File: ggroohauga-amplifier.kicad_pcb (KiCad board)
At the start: 2 copper layers, 90 x 31 mm, 9 parts

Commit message: Ground unused GPIOs
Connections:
- A-C1 pad 2: GND -> GPIO_L11_C11_M15
- A-C2 pad 2: GND -> GPIO_L11_C11_M15
- A-J1 pad 0: GND -> GPIO_L11_C11_M15
- A-J1 pad 6: GND -> GPIO_L11_C11_M15
- A-U1 pad 15: GND -> GPIO_L11_C11_M15
- A-U1 pad 2: GND -> GPIO_L11_C11_M15
- A-U1 pad 8: GND -> GPIO_L11_C11_M15
- A-U1 pad 9: GND -> GPIO_L11_C11_M15
- S3L1 pad 11: GPIO_L18_C18_M9 -> GPIO_L11_C11_M15
- S3L1 pad 18: GPIO_L12_C12_M16 -> GPIO_L11_C11_M15
- S3L1 pad 7: GND -> GPIO_L11_C11_M15
- S3L1 pad 8: GND -> GPIO_L11_C11_M15
- S3L1 pad 9: GND -> GPIO_L11_C11_M15
- S3R1 pad 1: GND -> GPIO_L11_C11_M15
- S3R1 pad 14: GPIO_L47_C47_M35 -> GPIO_L11_C11_M15
- S3R1 pad 15: GPIO_L21_C21_M21 -> GPIO_L11_C11_M15
- S3R1 pad 7: GPIO_L41_C41_M42 -> GPIO_L11_C11_M15
- S3R1 pad 9: GPIO_L39_C39_M40 -> GPIO_L11_C11_M15
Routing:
- net GPIO_L11_C11_M15: track 0.00 -> 9.52 mm, vias 0 -> 3
- net GND: track 9.52 -> 0.00 mm, vias 3 -> 0
- added copper zone on B.Cu, net GPIO_L11_C11_M15
- added copper zone on F.Cu, net GPIO_L11_C11_M15
- removed copper zone on B.Cu, net GND
- removed copper zone on F.Cu, net GND

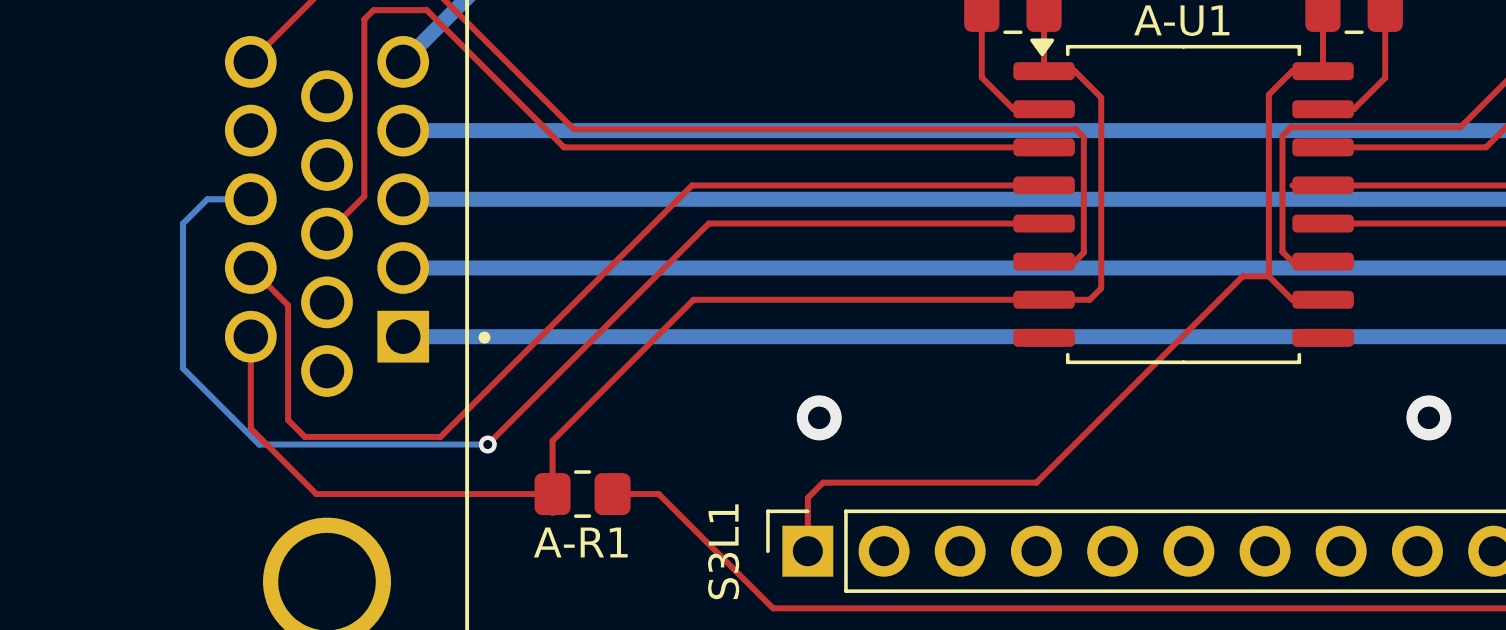
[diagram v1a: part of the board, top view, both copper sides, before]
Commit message: Move bridge text out of the way of vias and cleanup tracks
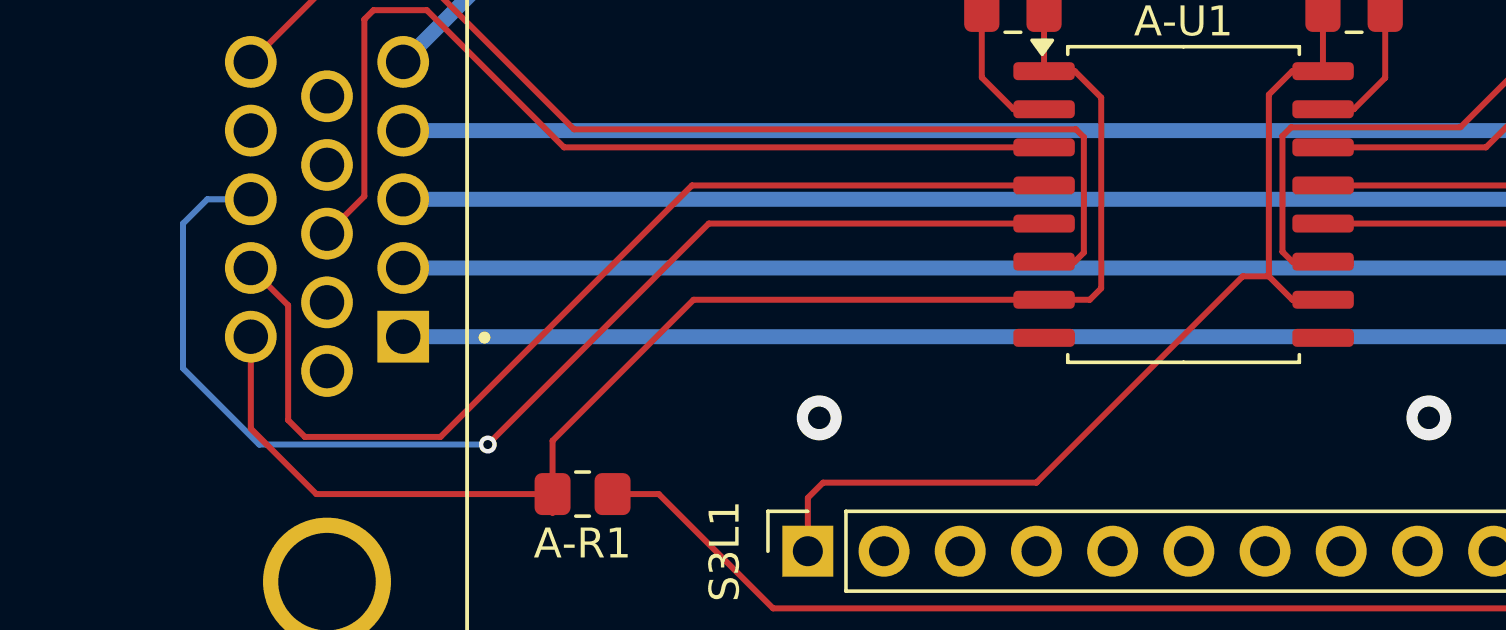
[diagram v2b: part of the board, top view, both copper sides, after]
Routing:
- net /Common/GPIO_L9_C9_M13/AMP_TX: track 25.2 -> 24.2 mm
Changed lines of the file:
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@@
 	)
 	(segment
-		(start 63.246 73.914)
-		(end 62.357 73.025)
-		(width 0.2)
-		(layer "B.Cu")
-		(net 6)
-	)
-	(segment
-		(start 62.357 73.025)
-		(end 60.706 71.374)
+		(start 60.706 71.374)
+		(end 63.246 73.914)
 		(width 0.2)
 		(layer "B.Cu")
@@
 	)
 	(segment
-		(start 98.708 65.278)
-		(end 97.683001 65.278)
-		(width 0.2)
-		(layer "F.Cu")
-		(net 17)
-	)
-	(segment
 		(start 97.683001 67.818)
 		(end 97.355001 67.49)
@@
 	)
 	(segment
-		(start 97.054 68.458999)
+		(start 96.901 68.305999)
 		(end 97.683001 69.088)
 		(width 0.2)
 		(layer "F.Cu")
-		(net 20)
-	)
-	(segment
-		(start 96.901 68.305999)
-		(end 97.054 68.458999)
-		(width 0.2)
-		(layer "F.Cu")

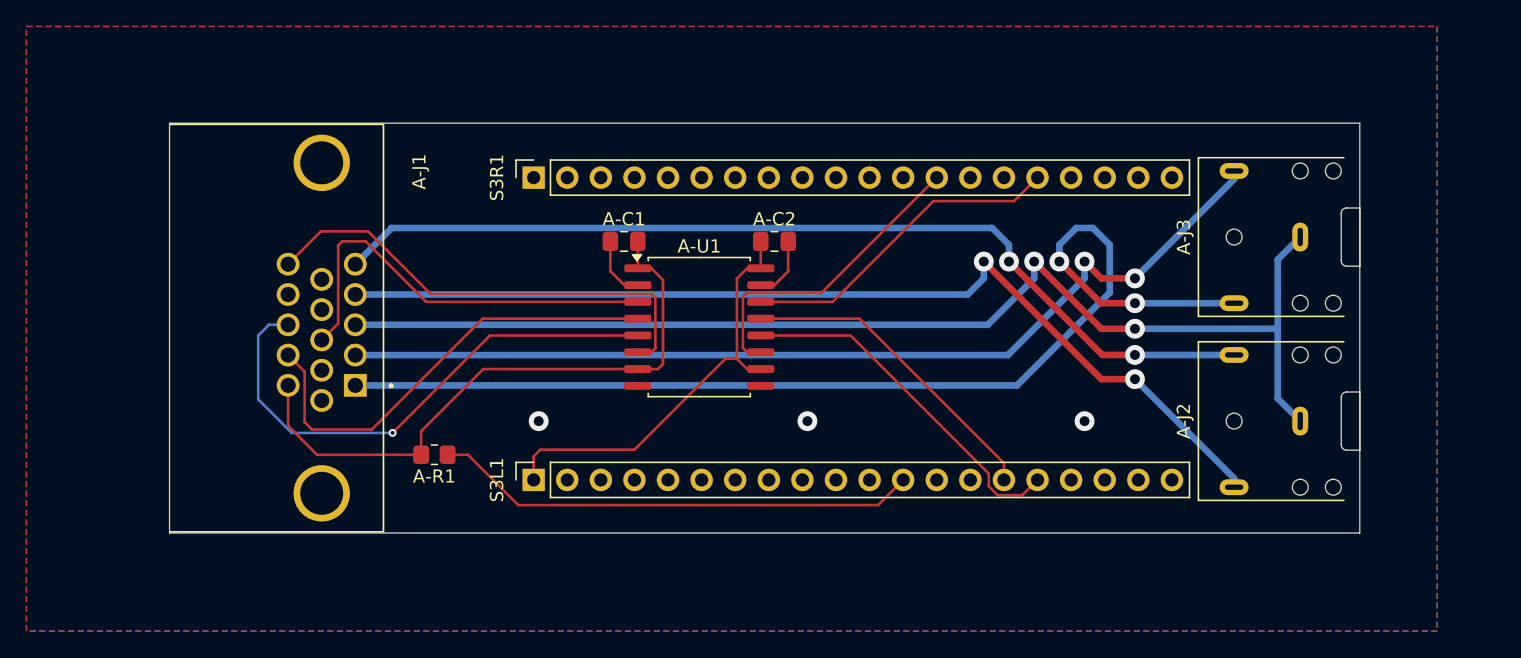
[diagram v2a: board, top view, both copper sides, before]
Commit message: Make amplifier PCB longer to accommodate the extra 2 pins on DevKit boards
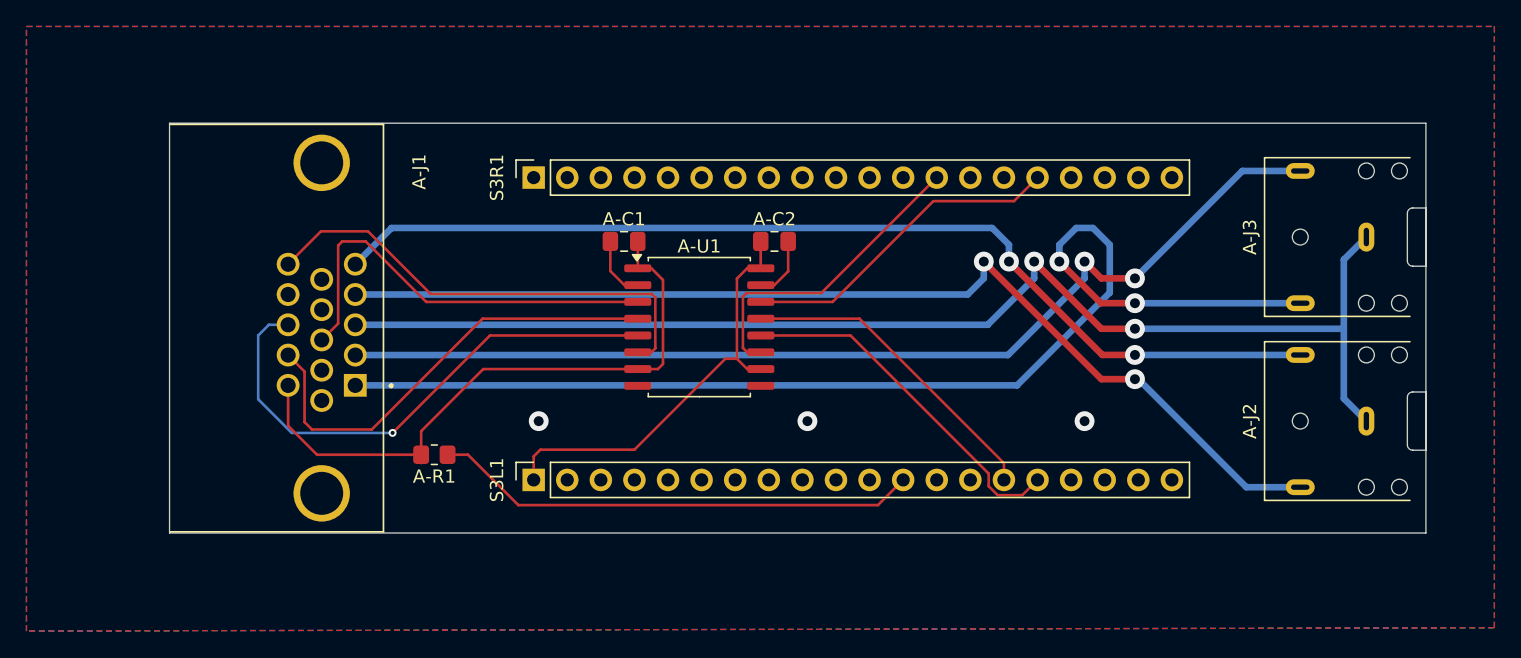
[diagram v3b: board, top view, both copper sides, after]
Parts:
- moved A-J2 5.00 mm to (144.5, 73.0)
- moved A-J3 5.00 mm to (144.5, 59.1)
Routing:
- net AUDIO_HEADPHONES_R: track 84.2 -> 89.2 mm
- net AUDIO_GROUND: track 89.9 -> 94.9 mm
- net AUDIO_AUX_L: track 72.3 -> 77.3 mm
- net AUDIO_HEADPHONES_L: track 74.4 -> 79.0 mm
- net AUDIO_AUX_R: track 75.7 -> 80.3 mm
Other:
- board size 90 x 31 mm -> 95 x 31 mm
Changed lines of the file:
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@@
 	(footprint "ggroohauga:Jack_3.5mm_CUI_SJ1-3523N_Horizontal"
 		(layer "F.Cu")
-		(at 139.499848 59.1058 90)
+		(at 144.499848 59.1058 90)
 		(descr "TRS 3.5mm, horizontal, through-hole, https://www.cuidevices.com/product/resource/pdf/sj1-352xn.pdf")
 		(tags "TRS audio jack stereo horizontal")
@@
 	(footprint "ggroohauga:Jack_3.5mm_CUI_SJ1-3523N_Horizontal"
 		(layer "F.Cu")
-		(at 139.499848 73.01992 90)
+		(at 144.499848 73.01992 90)
 		(descr "TRS 3.5mm, horizontal, through-hole, https://www.cuidevices.com/product/resource/pdf/sj1-352xn.pdf")
 		(tags "TRS audio jack stereo horizontal")
@@
 	(gr_rect
 		(start 54 50.4952)
-		(end 144 81.4832)
+		(end 149 81.4832)
 		(stroke
 			(width 0.0254)
@@
 		)
 	)
+	(dimension
+		(type orthogonal)
+		(layer "Cmts.User")
+		(pts
+			(xy 125.984 77.47) (xy 131.064 77.47)
+		)
+		(height 9.144)
+		(orientation 0)
+		(format
+			(prefix "")
+			(suffix "")
+			(units 0)
+			(units_format 1)
+			(precision 1)
+		)
+		(style
+			(thickness 0.2)
+			(arrow_length 1.27)
+			(text_position_mode 0)
+			(arrow_direction outward)
+			(extension_height 0.58642)
+			(extension_offset 0.5)
+			(keep_text_aligned yes)
+		)
+		(gr_text "0.2 in"
+			(at 128.524 84.814 0)
+			(layer "Cmts.User")
+			(effects
+				(font
+					(size 1.5 1.5)
+					(thickness 0.3)
+				)
+			)
+		)
+	)
+	(dimension
+		(type orthogonal)
+		(layer "Cmts.User")
+		(pts
+			(xy 136.144 77.47) (xy 131.064 77.47)
+		)
+		(height 12.7)
+		(orientation 0)
+		(format
+			(prefix "")
+			(suffix "")
+			(units 0)
+			(units_format 1)
+			(precision 1)
+		)
+		(style
+			(thickness 0.2)
+			(arrow_length 1.27)
+			(text_position_mode 0)
+			(arrow_direction outward)
+			(extension_height 0.58642)
+			(extension_offset 0.5)
+			(keep_text_aligned yes)
+		)
+		(gr_text "0.2 in"
+			(at 133.604 88.37 0)
+			(layer "Cmts.User")
+			(effects
+				(font
+					(size 1.5 1.5)
+					(thickness 0.3)
+				)
+			)
+		)
+	)
+	(dimension
+		(type orthogonal)
+		(layer "Cmts.User")
+		(pts
+			(xy 131.064 54.61) (xy 136.144 54.61)
+		)
+		(height -11.938)
+		(orientation 0)
+		(format
+			(prefix "")
+			(suffix "")
+			(units 0)
+			(units_format 1)
+			(precision 1)
+		)
+		(style
+			(thickness 0.2)
+			(arrow_length 1.27)
+			(text_position_mode 0)
+			(arrow_direction outward)
+			(extension_height 0.58642)
+			(extension_offset 0.5)
+			(keep_text_aligned yes)
+		)
+		(gr_text "0.2 in"
+			(at 133.604 40.872 0)
+			(layer "Cmts.User")
+			(effects
+				(font
+					(size 1.5 1.5)
+					(thickness 0.3)
+				)
+			)
+		)
+	)
+	(dimension
+		(type orthogonal)
+		(layer "Cmts.User")
+		(pts
+			(xy 131.064 54.61) (xy 125.984 54.61)
+		)
+		(height -9.144)
+		(orientation 0)
+		(format
+			(prefix "")
+			(suffix "")
+			(units 0)
+			(units_format 1)
+			(precision 1)
+		)
+		(style
+			(thickness 0.2)
+			(arrow_length 1.27)
+			(text_position_mode 0)
+			(arrow_direction outward)
+			(extension_height 0.58642)
+			(extension_offset 0.5)
+			(keep_text_aligned yes)
+		)
+		(gr_text "0.2 in"
+			(at 128.524 43.666 0)
+			(layer "Cmts.User")
+			(effects
+				(font
+					(size 1.5 1.5)
+					(thickness 0.3)
+				)
+			)
+		)
+	)
 	(segment
 		(start 124.53492 68.01992)
@@
 	)
 	(segment
-		(start 127 68.01992)
-		(end 134.499848 68.01992)
+		(start 116.205 58.42)
+		(end 70.7854 58.42)
 		(width 0.5)
 		(layer "B.Cu")
@@
 	)
 	(segment
-		(start 116.205 58.42)
-		(end 70.7854 58.42)
+		(start 117.475 60.96)
+		(end 117.475 59.69)
 		(width 0.5)
 		(layer "B.Cu")
@@
 	)
 	(segment
-		(start 117.475 60.96)
-		(end 117.475 59.69)
+		(start 127 68.01992)
+		(end 139.499848 68.01992)
 		(width 0.5)
 		(layer "B.Cu")
@@
 	)
 	(segment
-		(start 134.499848 77.349848)
-		(end 134.499848 78.01992)
-		(width 0.5)
-		(layer "B.Cu")
-		(net 8)
-	)
-	(segment
 		(start 114.3508 63.4492)
 		(end 68.0462 63.4492)
@@
 	(segment
 		(start 127 69.85)
-		(end 134.499848 77.349848)
+		(end 127.254 69.85)
+		(width 0.5)
+		(layer "B.Cu")
+		(net 8)
+	)
+	(segment
+		(start 135.42392 78.01992)
+		(end 139.499848 78.01992)
 		(width 0.5)
 		(layer "B.Cu")
@@
 	)
 	(segment
+		(start 127.254 69.85)
+		(end 135.42392 78.01992)
+		(width 0.5)
+		(layer "B.Cu")
+		(net 8)
+	)
+	(segment
 		(start 127 66.04)
 		(end 124.46 66.04)
@@
 	)
 	(segment
-		(start 137.795 66.04)
-		(end 137.795 71.315072)
+		(start 142.795 66.04)
+		(end 142.795 71.315072)
 		(width 0.5)
 		(layer "B.Cu")
@@
 	)
 	(segment
-		(start 119.38 62.23)
-		(end 115.8708 65.7392)
+		(start 142.795 60.810648)
+		(end 144.499848 59.1058)
 		(width 0.5)
 		(layer "B.Cu")
@@
 	)
 	(segment
-		(start 137.795 60.810648)
-		(end 137.795 66.04)
+		(start 119.38 62.23)
+		(end 115.8708 65.7392)
 		(width 0.5)
 		(layer "B.Cu")
@@
 	)
 	(segment
-		(start 127 66.04)
-		(end 137.795 66.04)
+		(start 142.795 71.315072)
+		(end 144.499848 73.01992)
 		(width 0.5)
 		(layer "B.Cu")
@@
 	)
 	(segment
-		(start 137.795 71.315072)
-		(end 139.499848 73.01992)
+		(start 142.795 60.810648)
+		(end 142.795 66.04)
 		(width 0.5)
 		(layer "B.Cu")
@@
 	)
 	(segment
-		(start 139.499848 59.1058)
-		(end 137.795 60.810648)
+		(start 127 66.04)
+		(end 142.795 66.04)
 		(width 0.5)
 		(layer "B.Cu")
@@
 	)
 	(segment
-		(start 134.499848 54.730152)
-		(end 134.499848 54.1058)
+		(start 123.19 60.96)
+		(end 123.19 62.23)
 		(width 0.5)
 		(layer "B.Cu")
@@
 	)
 	(segment
-		(start 127 62.23)
-		(end 134.499848 54.730152)
+		(start 123.19 62.23)
+		(end 117.3908 68.0292)
 		(width 0.5)
 		(layer "B.Cu")
@@
 	)
 	(segment
-		(start 123.19 60.96)
-		(end 123.19 62.23)
+		(start 117.3908 68.0292)
+		(end 68.0462 68.0292)
 		(width 0.5)
 		(layer "B.Cu")
@@
 	)
 	(segment
-		(start 123.19 62.23)
-		(end 117.3908 68.0292)
+		(start 127 62.23)
+		(end 135.1242 54.1058)
 		(width 0.5)
 		(layer "B.Cu")
@@
 	)
 	(segment
-		(start 117.3908 68.0292)
-		(end 68.0462 68.0292)
+		(start 135.1242 54.1058)
+		(end 139.499848 54.1058)
 		(width 0.5)
 		(layer "B.Cu")
@@
 	(segment
 		(start 127 64.1058)
-		(end 134.499848 64.1058)
+		(end 139.499848 64.1058)
 		(width 0.5)
 		(layer "B.Cu")
@@
 		(polygon
 			(pts
-				(xy 43.18 43.18) (xy 149.86 43.18) (xy 149.86 88.9) (xy 43.18 88.9)
+				(xy 43.18 43.18) (xy 154.178 43.18) (xy 154.178 88.646) (xy 43.18 88.9)
 			)
 		)

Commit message: Add "BOARD_ID" to the GPIOs for that and fix net names on unused GPIOs
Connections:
- net GPIO_L11_C11_M15 renamed GND
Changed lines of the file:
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@@
 	(net 42 "unconnected-(S3R1-Pin_19-Pad19)")
 	(net 43 "unconnected-(S3L1-Pin_2-Pad2)")
-	(net 44 "GPIO_L11_C11_M15")
+	(net 44 "GND")
 	(footprint "Connector_PinSocket_2.54mm:PinSocket_1x20_P2.54mm_Vertical"
 		(layer "F.Cu")
@@
 			(layers "*.Cu" "*.Mask")
 			(remove_unused_layers no)
-			(net 44 "GPIO_L11_C11_M15")
+			(net 44 "GND")
 			(pinfunction "Pin_1")
 			(pintype "passive")
@@
 			(layers "*.Cu" "*.Mask")
 			(remove_unused_layers no)
-			(net 44 "GPIO_L11_C11_M15")
+			(net 44 "GND")
 			(pinfunction "Pin_7")
 			(pintype "passive")
@@
 			(layers "*.Cu" "*.Mask")
 			(remove_unused_layers no)
-			(net 44 "GPIO_L11_C11_M15")
+			(net 44 "GND")
 			(pinfunction "Pin_9")
 			(pintype "passive")
@@
 			(layers "*.Cu" "*.Mask")
 			(remove_unused_layers no)
-			(net 44 "GPIO_L11_C11_M15")
+			(net 44 "GND")
 			(pinfunction "Pin_14")
 			(pintype "passive")
@@
 			(layers "*.Cu" "*.Mask")
 			(remove_unused_layers no)
-			(net 44 "GPIO_L11_C11_M15")
+			(net 44 "GND")
 			(pinfunction "Pin_15")
 			(pintype "passive")
@@
 			(layers "F.Cu" "F.Mask" "F.Paste")
 			(roundrect_rratio 0.212766)
-			(net 44 "GPIO_L11_C11_M15")
+			(net 44 "GND")
 			(pintype "passive")
 		)
@@
 			(layers "*.Cu" "*.Mask")
 			(remove_unused_layers no)
-			(net 44 "GPIO_L11_C11_M15")
+			(net 44 "GND")
 			(pinfunction "Pin_7")
 			(pintype "passive")
@@
 			(layers "*.Cu" "*.Mask")
 			(remove_unused_layers no)
-			(net 44 "GPIO_L11_C11_M15")
+			(net 44 "GND")
 			(pinfunction "Pin_8")
 			(pintype "passive")
@@
 			(layers "*.Cu" "*.Mask")
 			(remove_unused_layers no)
-			(net 44 "GPIO_L11_C11_M15")
+			(net 44 "GND")
 			(pinfunction "Pin_9")
 			(pintype "passive")
@@
 			(layers "*.Cu" "*.Mask")
 			(remove_unused_layers no)
-			(net 44 "GPIO_L11_C11_M15")
+			(net 44 "GND")
 			(pinfunction "Pin_11")
 			(pintype "passive")
@@
 			(layers "*.Cu" "*.Mask")
 			(remove_unused_layers no)
-			(net 44 "GPIO_L11_C11_M15")
+			(net 44 "GND")
 			(pinfunction "Pin_17")
 			(pintype "passive")
@@
 			(layers "*.Cu" "*.Mask")
 			(remove_unused_layers no)
-			(net 44 "GPIO_L11_C11_M15")
+			(net 44 "GND")
 			(pinfunction "Pin_18")
 			(pintype "passive")
@@
 			(layers "F.Cu" "F.Mask" "F.Paste")
 			(roundrect_rratio 0.212766)
-			(net 44 "GPIO_L11_C11_M15")
+			(net 44 "GND")
 			(pintype "passive")
 		)
@@
 			(layers "F.Cu" "F.Mask" "F.Paste")
 			(roundrect_rratio 0.25)
-			(net 44 "GPIO_L11_C11_M15")
+			(net 44 "GND")
 			(pinfunction "GND1")
 			(pintype "power_in")
@@
 			(layers "F.Cu" "F.Mask" "F.Paste")
 			(roundrect_rratio 0.25)
-			(net 44 "GPIO_L11_C11_M15")
+			(net 44 "GND")
 			(pinfunction "GND1")
 			(pintype "passive")
@@
 			(layers "F.Cu" "F.Mask" "F.Paste")
 			(roundrect_rratio 0.25)
-			(net 44 "GPIO_L11_C11_M15")
+			(net 44 "GND")
 			(pinfunction "GND2")
 			(pintype "power_in")
@@
 			(layers "F.Cu" "F.Mask" "F.Paste")
 			(roundrect_rratio 0.25)
-			(net 44 "GPIO_L11_C11_M15")
+			(net 44 "GND")
 			(pinfunction "GND2")
 			(pintype "passive")
@@
 			(layers "*.Cu" "*.Mask")
 			(remove_unused_layers no)
-			(net 44 "GPIO_L11_C11_M15")
+			(net 44 "GND")
 			(pintype "passive")
 			(solder_mask_margin 0.102)
@@
 			(layers "*.Cu" "*.Mask")
 			(remove_unused_layers no)
-			(net 44 "GPIO_L11_C11_M15")
+			(net 44 "GND")
 			(pintype "passive")
 			(solder_mask_margin 0.102)
@@
 			(layers "*.Cu" "*.Mask")
 			(remove_unused_layers no)
-			(net 44 "GPIO_L11_C11_M15")
+			(net 44 "GND")
 			(pintype "passive")
 			(solder_mask_margin 0.102)
@@
 	(zone
 		(net 44)
-		(net_name "GPIO_L11_C11_M15")
+		(net_name "GND")
 		(layers "F.Cu" "B.Cu")
 		(hatch edge 0.5)
